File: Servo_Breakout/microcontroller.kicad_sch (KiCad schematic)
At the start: 9 parts, among them U201 STM32L412CBTx

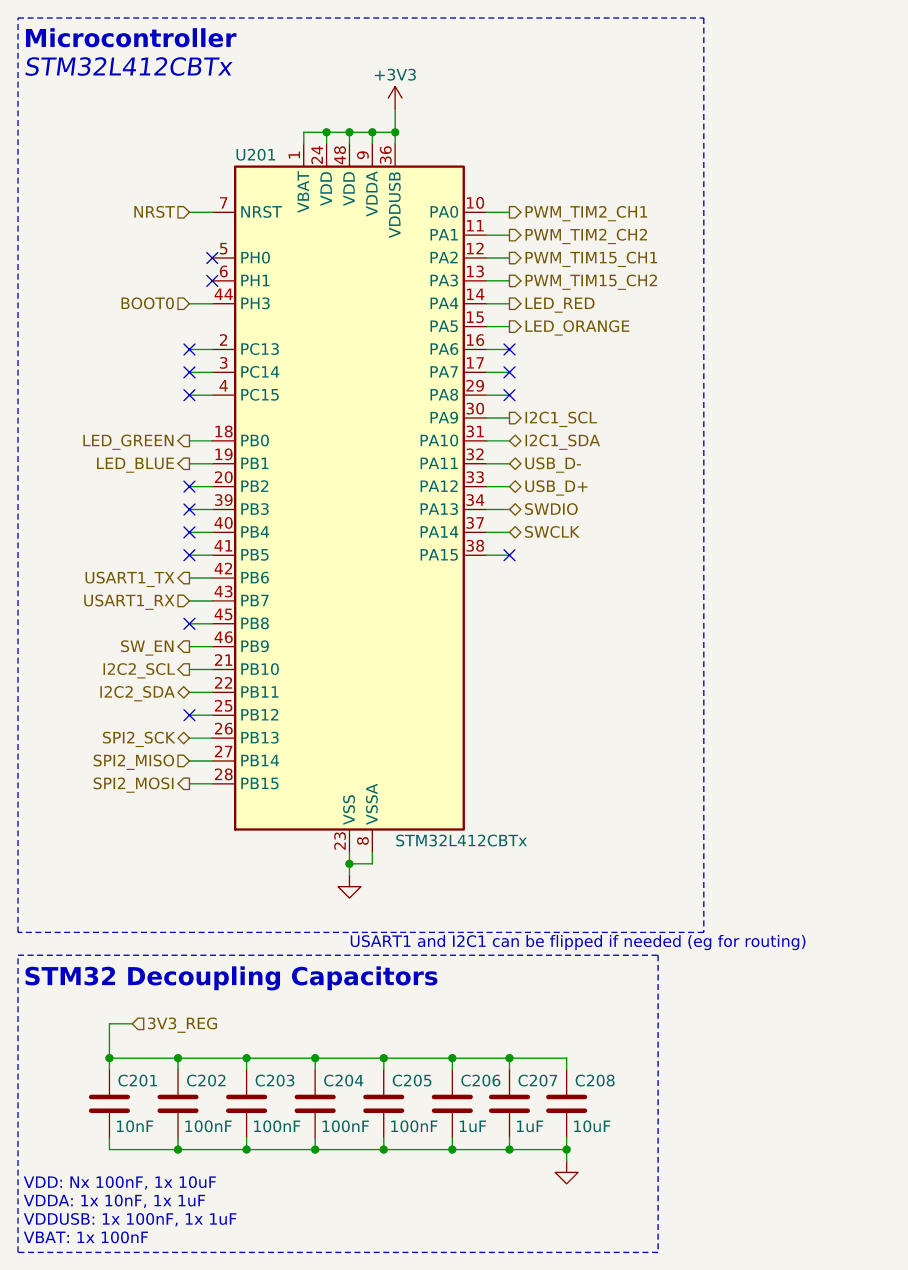
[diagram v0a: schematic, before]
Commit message: finalized schematic. footprints in progress
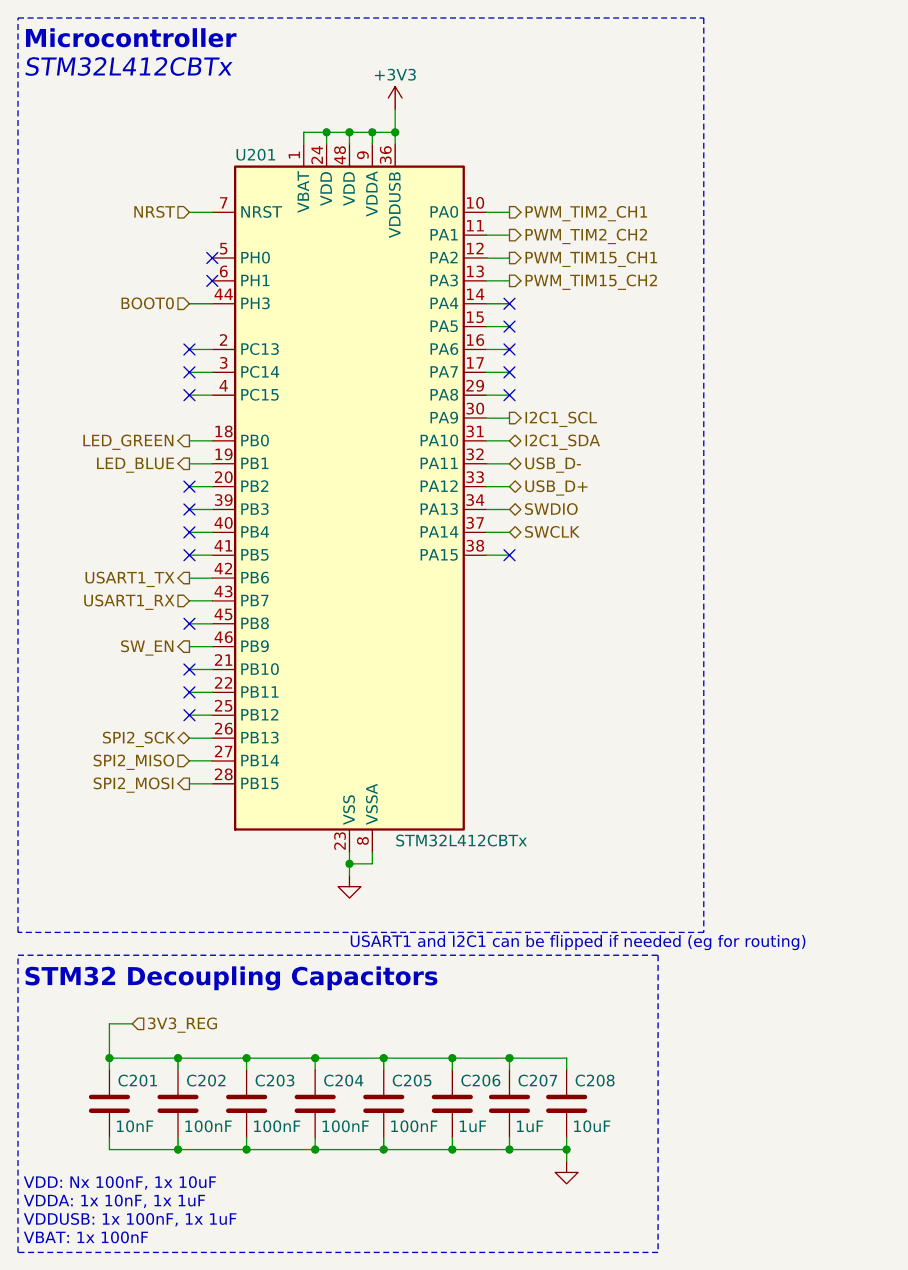
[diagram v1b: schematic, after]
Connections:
- net I2C2_SCL: no longer names the net of U201.21 (PB10)
- net I2C2_SDA: no longer names the net of U201.22 (PB11)
- net LED_ORANGE: no longer names the net of U201.15 (PA5)
- net LED_RED: no longer names the net of U201.14 (PA4)
- no-connect marks 15 -> 19
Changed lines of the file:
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@@
+	)
+	(no_connect
+		(at 34.29 87.63)
 	)
 	(no_connect
@@
 	)
 	(no_connect
+		(at 69.85 46.99)
+	)
+	(no_connect
 		(at 34.29 69.85)
 	)
@@
 	)
 	(no_connect
+		(at 69.85 49.53)
+	)
+	(no_connect
 		(at 69.85 52.07)
 	)
 	(no_connect
+		(at 34.29 90.17)
+	)
+	(no_connect
 		(at 69.85 54.61)
 	)
@@
 	(wire
 		(pts
-			(xy 36.83 87.63) (xy 34.29 87.63)
-		)
-		(stroke
-			(width 0)
-			(type default)
-		)
-	)
-	(wire
-		(pts
 			(xy 67.31 41.91) (xy 69.85 41.91)
 		)
@@
 	(wire
 		(pts
+			(xy 34.29 90.17) (xy 36.83 90.17)
+		)
+		(stroke
+			(width 0)
+			(type default)
+		)
+	)
+	(wire
+		(pts
 			(xy 76.2 130.81) (xy 76.2 132.08)
 		)
@@
 	(wire
 		(pts
-			(xy 34.29 90.17) (xy 36.83 90.17)
-		)
-		(stroke
-			(width 0)
-			(type default)
-		)
-	)
-	(wire
-		(pts
 			(xy 55.88 130.81) (xy 55.88 132.08)
 		)
@@
 		(pts
 			(xy 54.61 27.94) (xy 52.07 27.94)
+		)
+		(stroke
+			(width 0)
+			(type default)
+		)
+	)
+	(wire
+		(pts
+			(xy 34.29 87.63) (xy 36.83 87.63)
 		)
 		(stroke
@@
 		)
 	)
-	(hierarchical_label "I2C2_SCL"
-		(shape output)
-		(at 34.29 87.63 180)
-		(effects
-			(font
-				(size 1.27 1.27)
-				(thickness 0.1588)
-			)
-			(justify right)
-		)
-	)
 	(hierarchical_label "BOOT0"
 		(shape input)
@@
 		)
 	)
-	(hierarchical_label "I2C2_SDA"
-		(shape bidirectional)
-		(at 34.29 90.17 180)
-		(effects
-			(font
-				(size 1.27 1.27)
-				(thickness 0.1588)
-			)
-			(justify right)
-		)
-	)
 	(hierarchical_label "SPI2_MISO"
 		(shape input)
@@
 		)
 	)
-	(hierarchical_label "LED_RED"
-		(shape output)
-		(at 69.85 46.99 0)
-		(effects
-			(font
-				(size 1.27 1.27)
-			)
-			(justify left)
-		)
-	)
 	(hierarchical_label "LED_GREEN"
 		(shape output)
@@
 		)
 	)
-	(hierarchical_label "LED_ORANGE"
-		(shape output)
-		(at 69.85 49.53 0)
-		(effects
-			(font
-				(size 1.27 1.27)
-			)
-			(justify left)
-		)
-	)
